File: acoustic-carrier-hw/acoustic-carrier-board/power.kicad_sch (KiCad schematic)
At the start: 79 parts, among them IC1 ECP5-BGA256, J3 Conn_02x08_Odd_Even, U10 TLV62569DRL, U11 TLV62569DRL, U12 TLV62569DRL, U8 TLV62569DRL

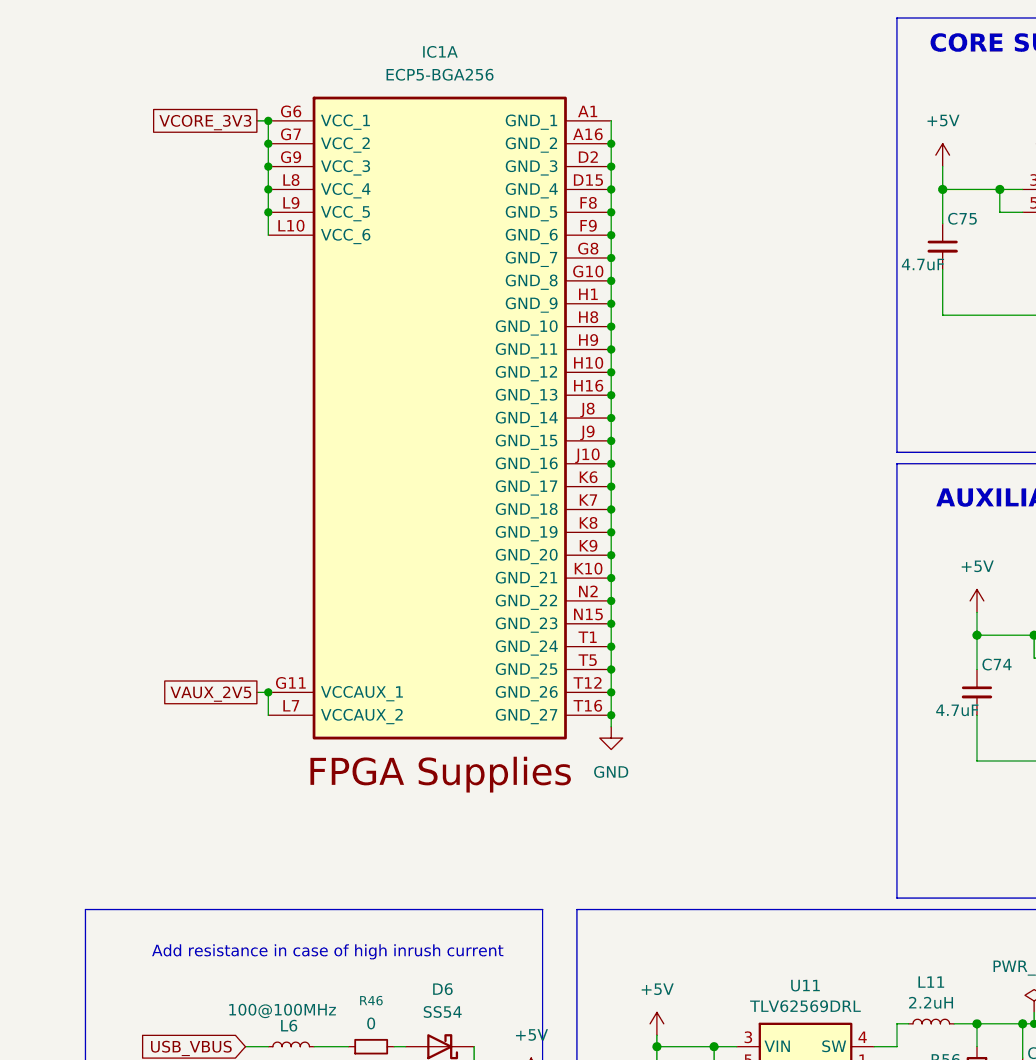
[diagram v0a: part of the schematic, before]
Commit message: [carrier] Finished flash and config check
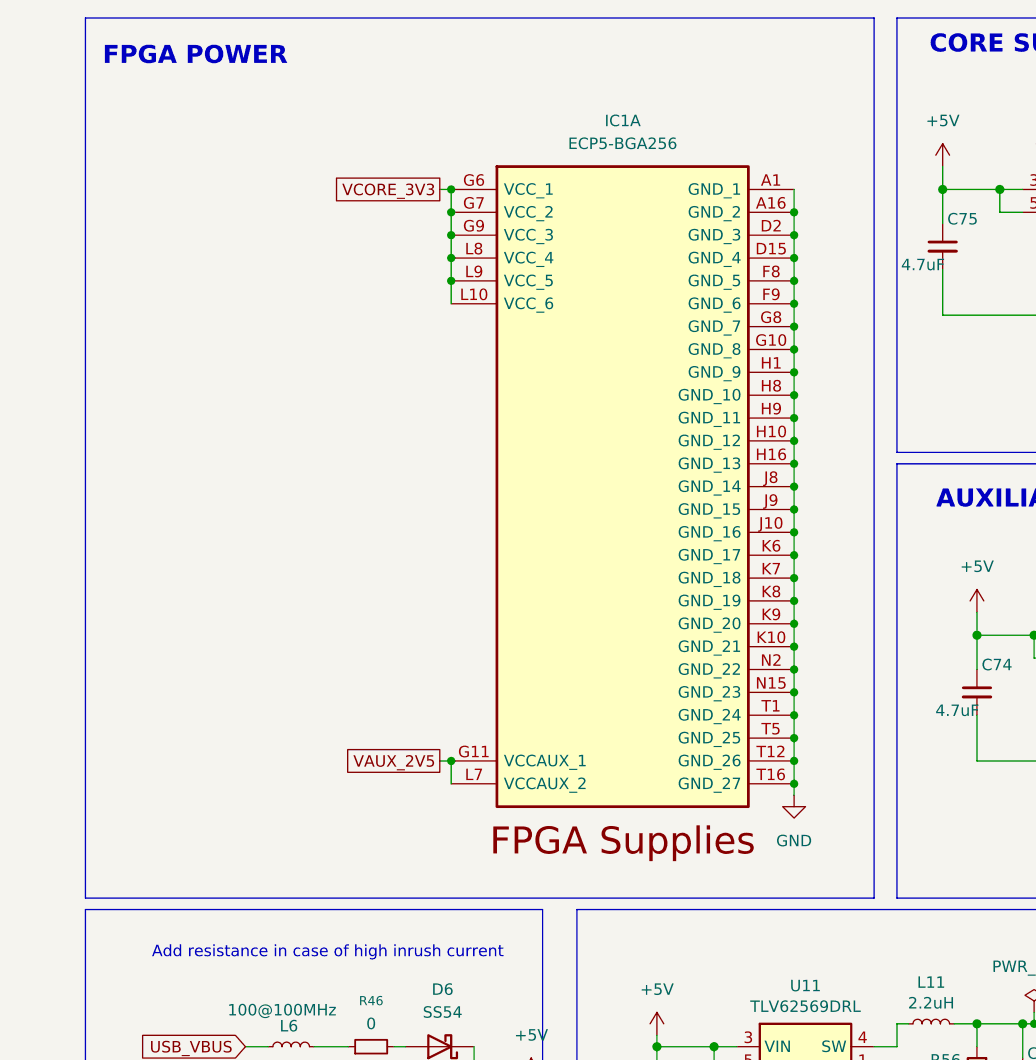
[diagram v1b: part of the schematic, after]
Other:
- note added: "FPGA POWER"
- moved on the sheet: IC1A

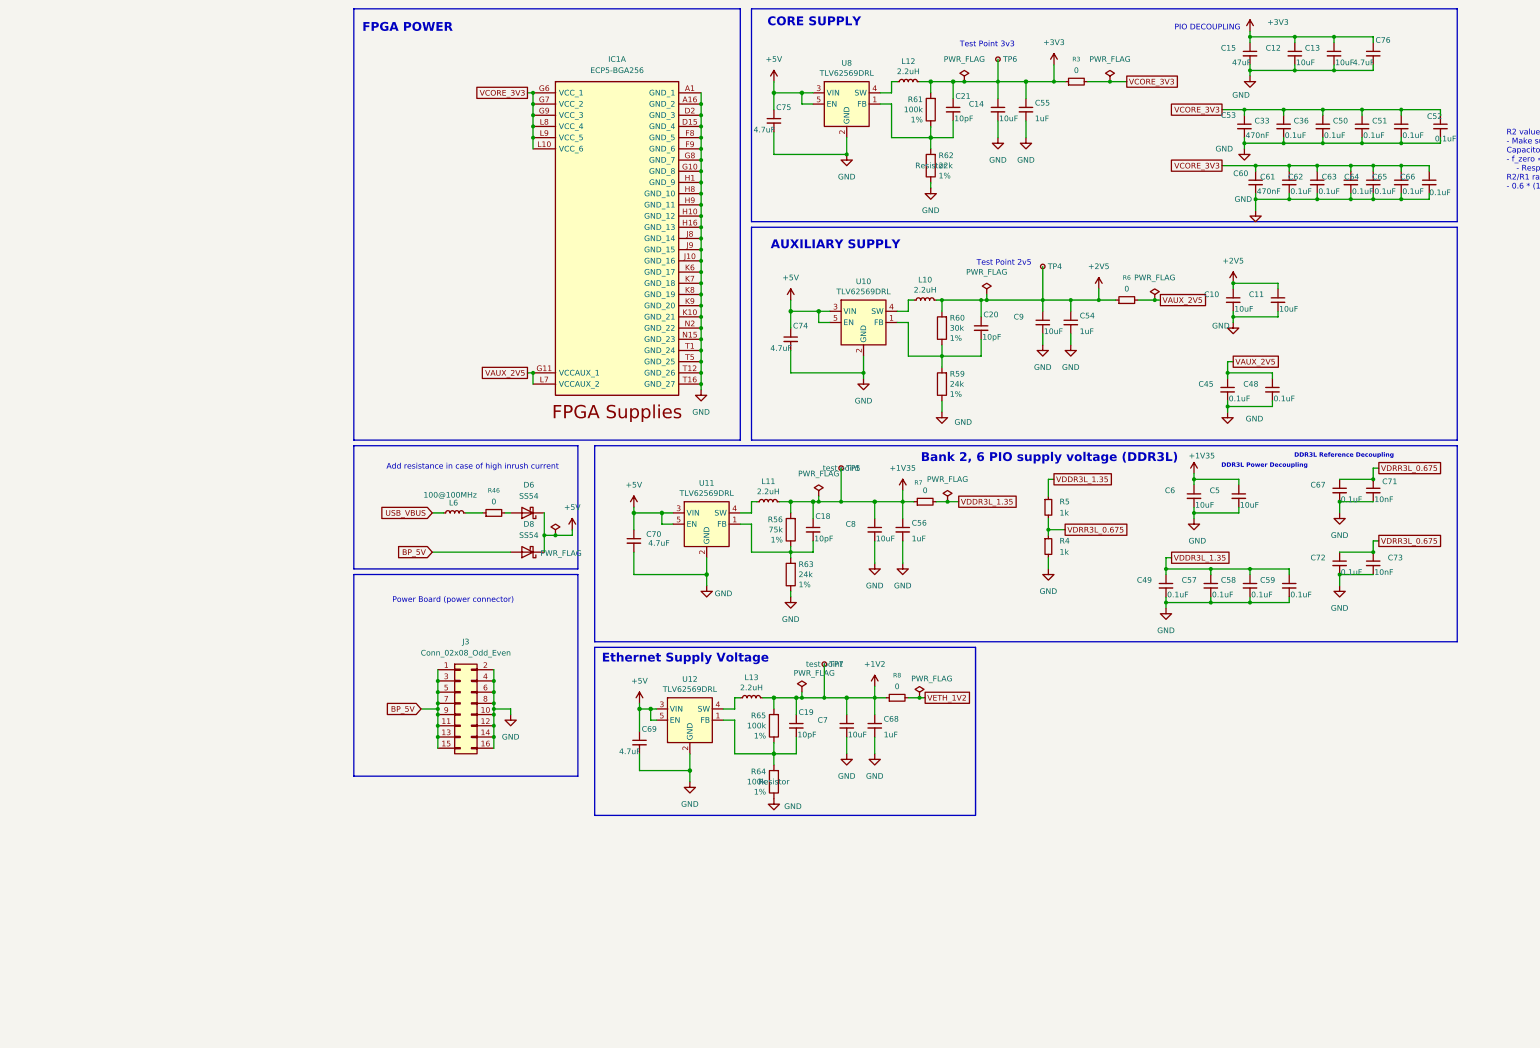
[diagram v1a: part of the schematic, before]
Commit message: [carrier] Further verification of power board (next) Replace ddr3l reference voltage using TPS51200
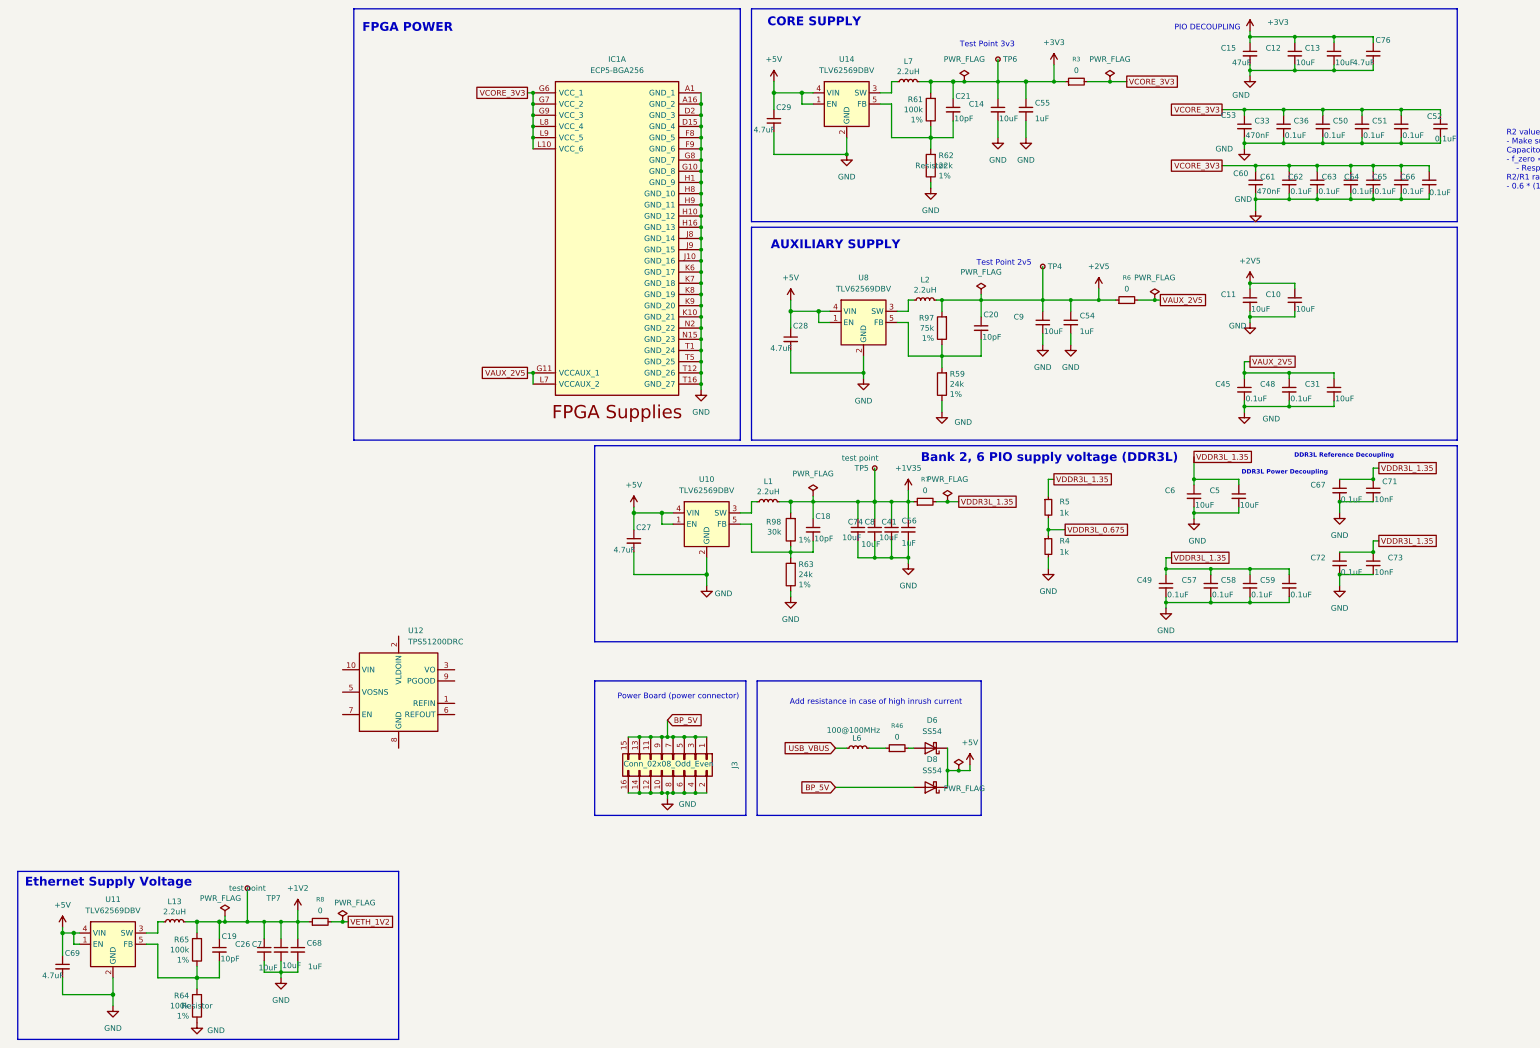
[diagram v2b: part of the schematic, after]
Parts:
- removed C70, C75: 4.7uF, Capacitor_SMD:C_0402_1005Metric, symbol Device:C_Small
- removed L10, L11, L12: 2.2uH, Inductor_SMD:L_0805_2012Metric, symbol Device:L_Small
- removed R56: 75k, Resistor_SMD:R_0603_1608Metric, symbol Device:R
- removed R60: 30k, Resistor_SMD:R_0603_1608Metric, symbol Device:R
- removed U10, U11, U12, U8: TLV62569DRL, Package_TO_SOT_SMD:SOT-563, symbol Regulator_Switching:TLV62569DRL
- added C26, C31, C41: 10uF, Capacitor_SMD:C_0603_1608Metric, symbol Device:C_Small
- added C27, C28, C29: 4.7uF, Capacitor_SMD:C_0402_1005Metric, symbol Device:C_Small
- added L1, L2, L7: 2.2uH, fpga:L_Changjiang_FNR4018S, symbol Device:L_Small
- added R97: 75k, Resistor_SMD:R_0603_1608Metric, symbol Device:R
- added R98: 30k, Resistor_SMD:R_0603_1608Metric, symbol Device:R
- added U10, U11, U14, U8: TLV62569DBV, Package_TO_SOT_SMD:SOT-23-5, symbol Regulator_Switching:TLV62569DBV
- added U12: TPS51200DRC, Package_SON:VSON-10-1EP_3x3mm_P0.5mm_EP1.65x2.4mm, symbol Regulator_Linear:TPS51200DRC
- C74: value 4.7uF -> 10uF; footprint Capacitor_SMD:C_0402_1005Metric -> Capacitor_SMD:C_0603_1608Metric; LPN C23733 -> C19702; MPN CL05A475MP5NRNC -> CL10A106KP8NNNC
- L13: footprint Inductor_SMD:L_0805_2012Metric -> fpga:L_Changjiang_FNR4018S
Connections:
- net +1V2: now also C26.1
- net +1V35: now also C74.1, C41.1, L1.2, R98.2; no longer C5.1, C6.1
- net +2V5: now also L2.2, R97.2
- net +3V3: now also L7.2
- net +5V: now also C27.1, C28.1, C29.1, U10.1 (EN), U10.4 (VIN), U11.1 (EN), U11.4 (VIN), U14.1 (EN), U14.4 (VIN), U8.1 (EN), U8.4 (VIN); no longer C74.1
- net GND: now also C26.2, C27.2, C28.2, C29.2, C31.2, C41.2, U10.2 (GND), U11.2 (GND), U14.2 (GND), U8.2 (GND)
- net VAUX_2V5: now also C31.1
- net VDDR3L_1.35: now also C5.1, C6.1, C67.1, C71.1, C72.1, C73.1
- net at C20.2, R59.2: now also R97.1, U8.5 (FB)
- net at C18.2, R63.2: now also R98.1, U10.5 (FB)
- net at C21.2, R61.1, R62.2: now also U14.5 (FB)
- net at L13.1: now also U11.3 (SW)
- net at C19.2, R64.2, R65.1: now also U11.5 (FB)
- removed net VDRR3L_0.675: C67.1, C71.1, C72.1, C73.1, R4.1, R5.2
- new net: L1.1, U10.3 (SW)
- new net: L7.1, U14.3 (SW)
- new net: L2.1, U8.3 (SW)
- new net: U12.11 (GND), U12.4 (GND), U12.8 (GND)
- new net VDDR3L_0.675: R4.1, R5.2
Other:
- moved on the sheet: C19, C45, C48, C56, C68, C69, C7, D6, D8, J3, L13, L6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

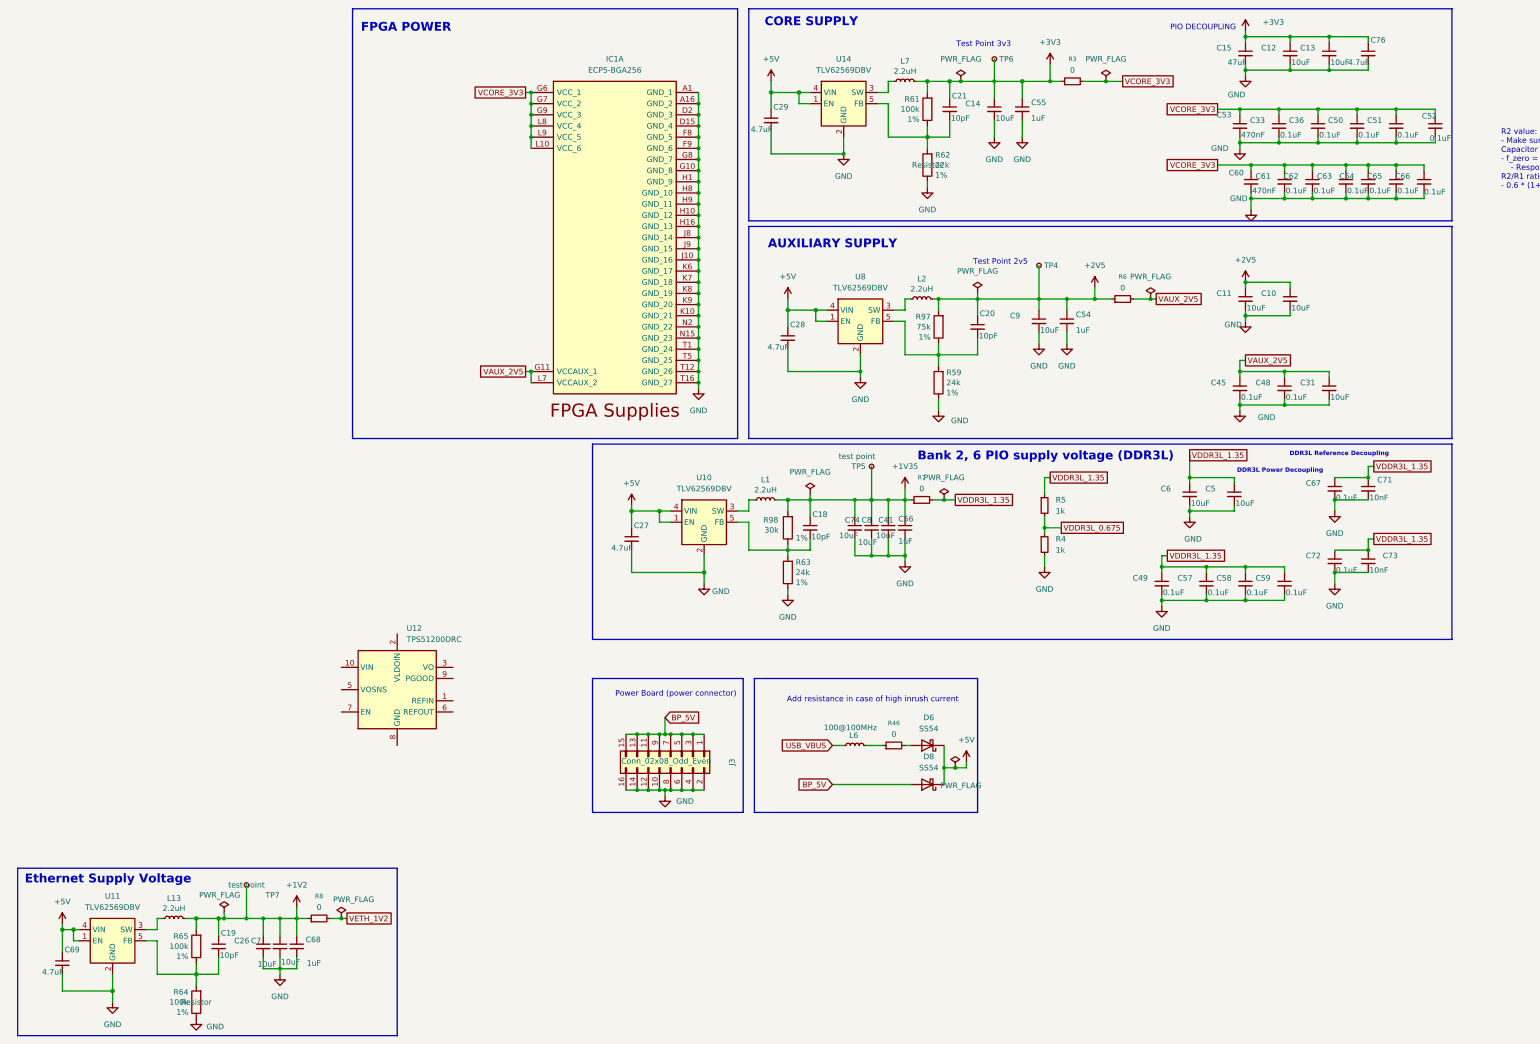
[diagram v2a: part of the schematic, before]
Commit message: [carrier] Added precision amplifier for DDRL voltage reference
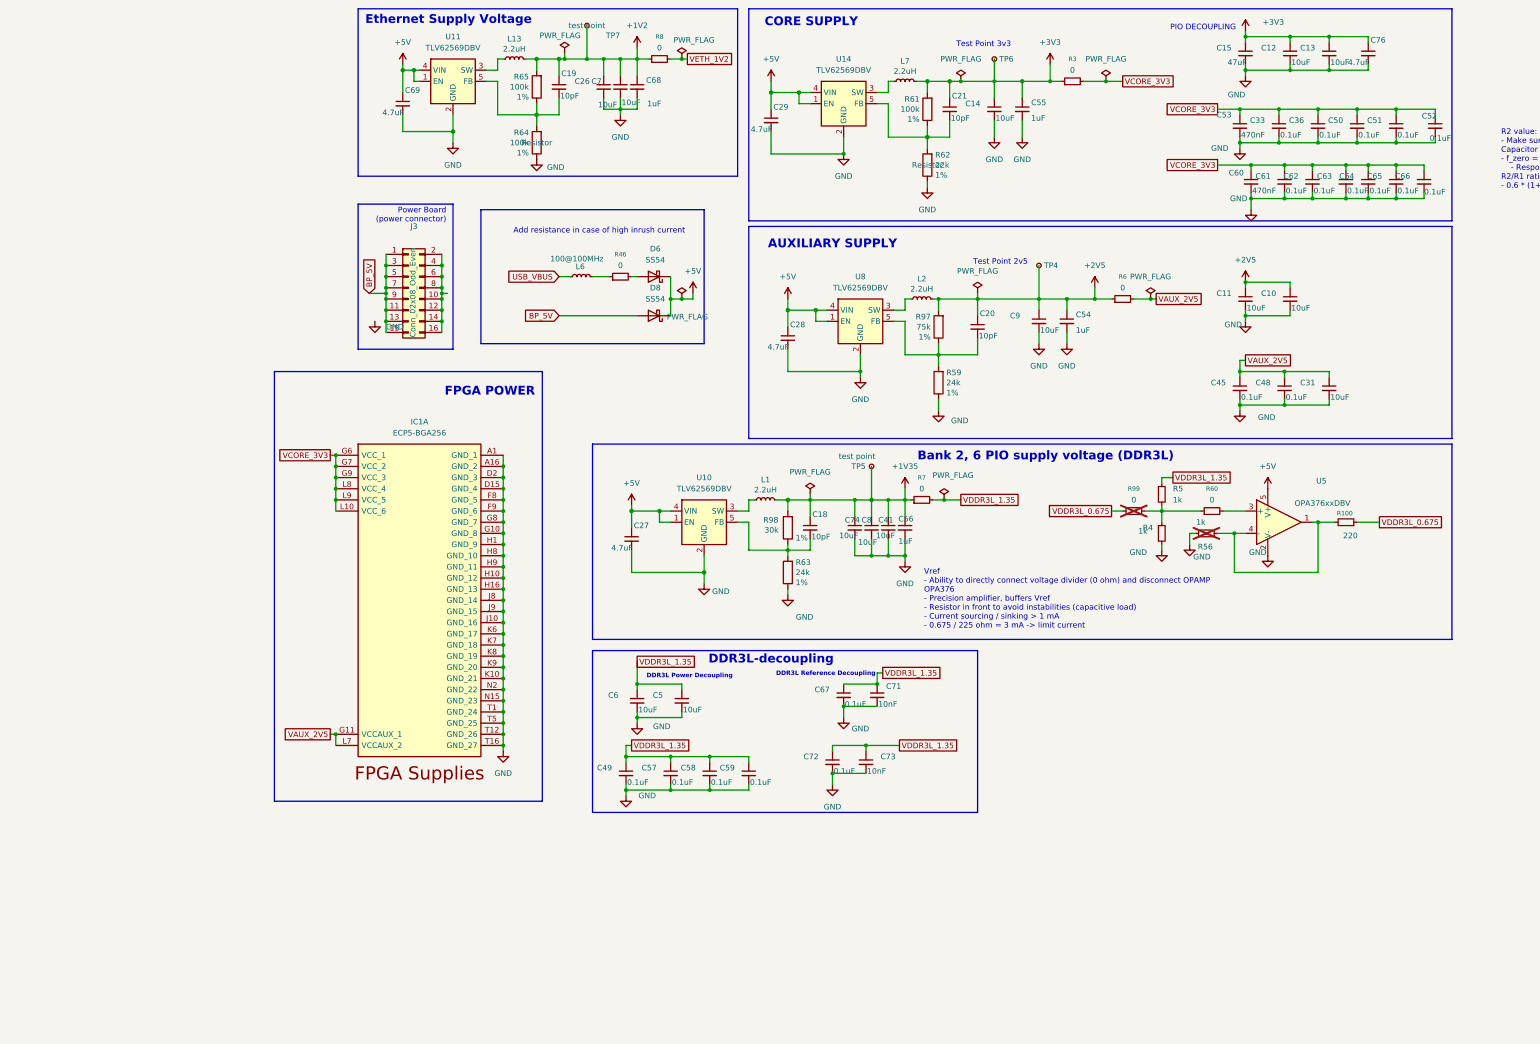
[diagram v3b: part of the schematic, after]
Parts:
- removed U12: TPS51200DRC, Package_SON:VSON-10-1EP_3x3mm_P0.5mm_EP1.65x2.4mm, symbol Regulator_Linear:TPS51200DRC
- added R100: 220, Resistor_SMD:R_0603_1608Metric, symbol Device:R_Small
- added R56: 1k, Resistor_SMD:R_0603_1608Metric, symbol Device:R_Small
- added R60, R99: 0, Resistor_SMD:R_0805_2012Metric_Pad1.20x1.40mm_HandSolder, symbol Device:R_Small
- added U5: OPA376xxDBV, Package_TO_SOT_SMD:SOT-23-5, symbol Amplifier_Operational:OPA376xxDBV
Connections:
- net +5V: now also U5.5 (V+)
- net GND: now also R56.1, U5.2 (V-); no longer J3.10 (Pin_10), J3.12 (Pin_12), J3.14 (Pin_14), J3.16 (Pin_16), J3.2 (Pin_2), J3.4 (Pin_4), J3.6 (Pin_6), J3.8 (Pin_8)
- net VDDR3L_0.675: now also R100.1, R99.1; no longer R4.1, R5.2
- new net: R100.2, R56.2, U5.1, U5.4 (-)
- new net: J3.10 (Pin_10), J3.12 (Pin_12), J3.14 (Pin_14), J3.16 (Pin_16), J3.2 (Pin_2), J3.4 (Pin_4), J3.6 (Pin_6), J3.8 (Pin_8)
- new net: R4.1, R5.2, R60.1, R99.2
- new net: R60.2, U5.3 (+)
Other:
- note added: "DDR3L-decoupling"
- note added: "Vref - Ability to directly connect voltage divider (0 ohm) and disconnect OPAMP OPA376 - Precision amplifier, buffers Vref - Resistor in front to avoid instabilities (capacitive load) - Current sourcing / sinking > 1 mA - 0.675 / 225 ohm = 3 mA -> limit current"
- moved on the sheet: C19, C26, C49, C5, C57, C58, C59, C6, C67, C68, C69, C7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
